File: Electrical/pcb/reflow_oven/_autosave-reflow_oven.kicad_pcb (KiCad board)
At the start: 2 copper layers, 64 parts, among them J1 1711738, J2 Conn_01x06, J3 DB9_Female, P1 USB_C_Receptacle_USB2.0, U1 LH05-10B05, U2 AP1117-33, U3 STM32F030CCTx, U4 CP2102N-Axx-xQFN28, U5 MAX485E, Y1 8MHz 8pF

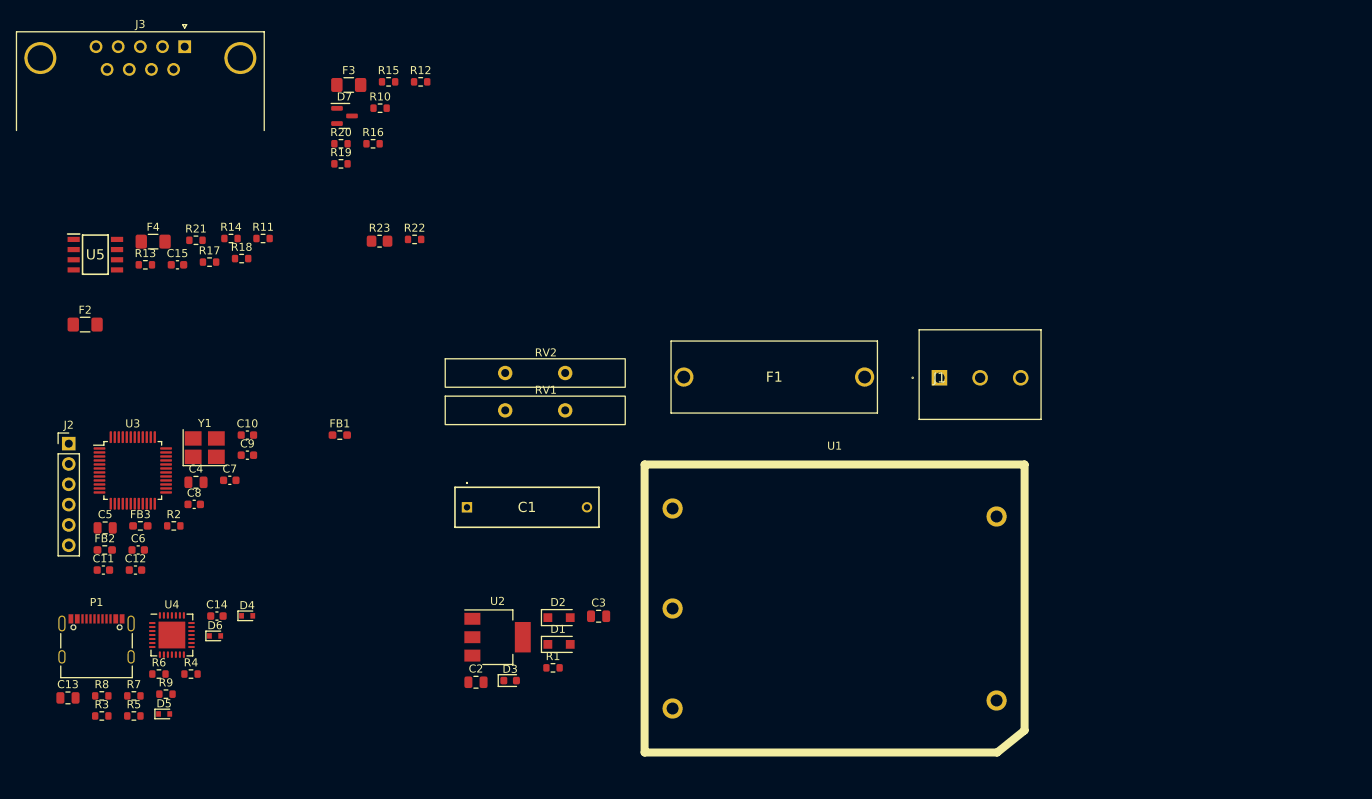
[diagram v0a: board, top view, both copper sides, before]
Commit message: interface
partial interface schematic
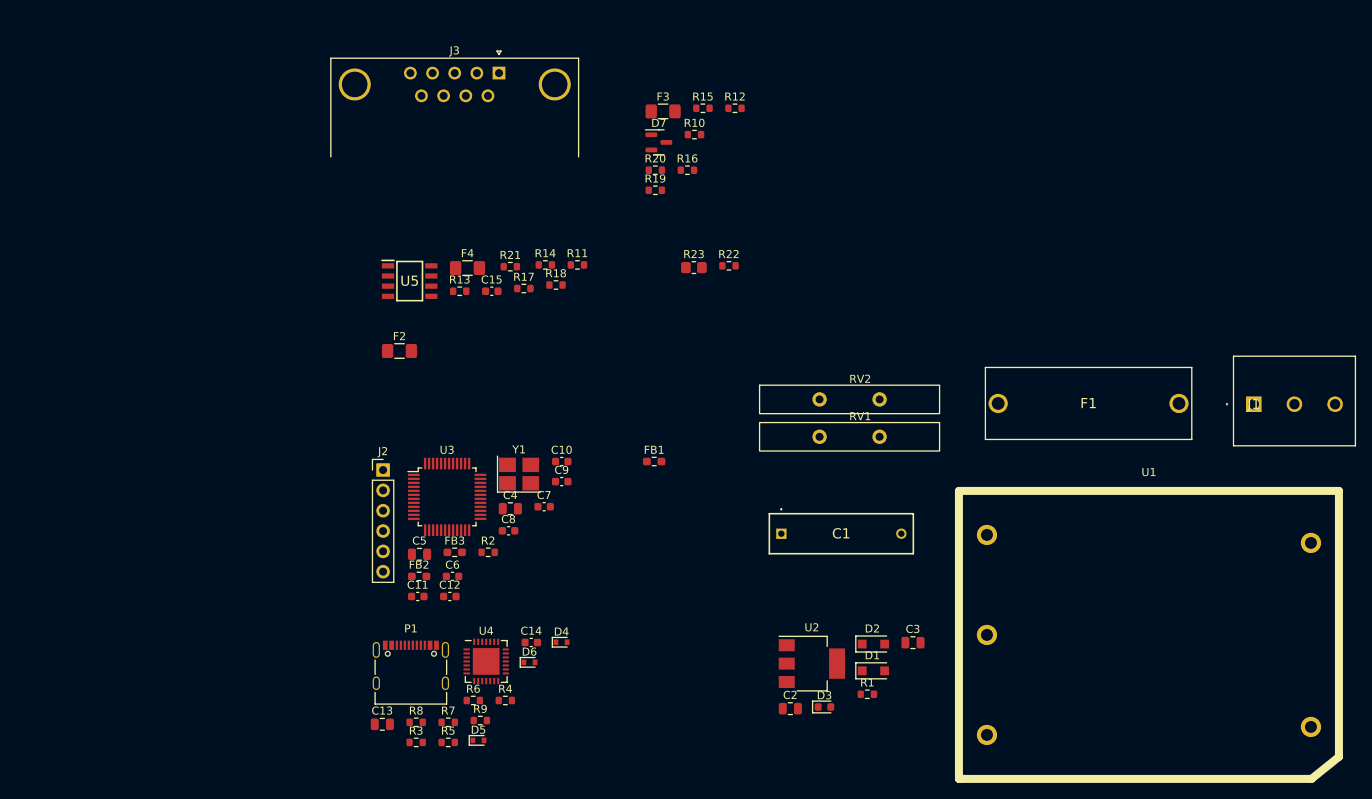
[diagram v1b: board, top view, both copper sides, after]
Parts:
- moved C1 39.4 mm to (-369.0, 37.2)
- moved C12 39.4 mm to (-410.4, 45.0)
- moved C13 39.4 mm to (-418.8, 61.0)
- moved C15 39.4 mm to (-405.2, 6.88)
- moved C2 39.4 mm to (-367.8, 59.1)
- moved C4 39.4 mm to (-402.8, 34.1)
- moved D5 39.4 mm to (-406.8, 63.0)
- moved D6 39.4 mm to (-400.5, 53.3)
- moved D7 39.4 mm to (-384.3, -11.7)
- moved J1 39.4 mm to (-309.9, 21.0)
- moved P1 39.4 mm to (-415.3, 53.6)
- moved R13 39.4 mm to (-409.2, 6.88)
- moved R14 39.4 mm to (-398.5, 3.59)
- moved R17 39.4 mm to (-401.1, 6.54)
- moved R19 39.4 mm to (-384.7, -5.74)
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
